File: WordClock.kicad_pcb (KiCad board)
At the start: 2 copper layers, 100 x 100 mm, 93 parts, among them J1 Conn_01x01, J2 Conn_01x01, J3 Conn_01x01, J4 Conn_01x09, J5 Conn_01x08, J6 Conn_01x08, J7 Conn_01x08, SW1 SW_Push, SW2 SW_Push, SW3 SW_Push, SW4 SW_Push, SW5 SW_Push, U1 AP1117-50, U10 NUD3124, U11 NUD3124, U12 NUD3124, U13 NUD3124, U14 NUD3124, U15 NUD3124, U16 NUD3124, U17 NUD3124, U18 NUD3124, U19 NUD3124, U2 AP1117-50, U20 NUD3124, U21 NUD3124, U22 NUD3124, U3 ARDUINO_NANO, U4 MCP7940N, U5 MCP23017, U6 MCP23017, U7 NUD3124, U8 NUD3124, U9 NUD3124, Y1 Crystal

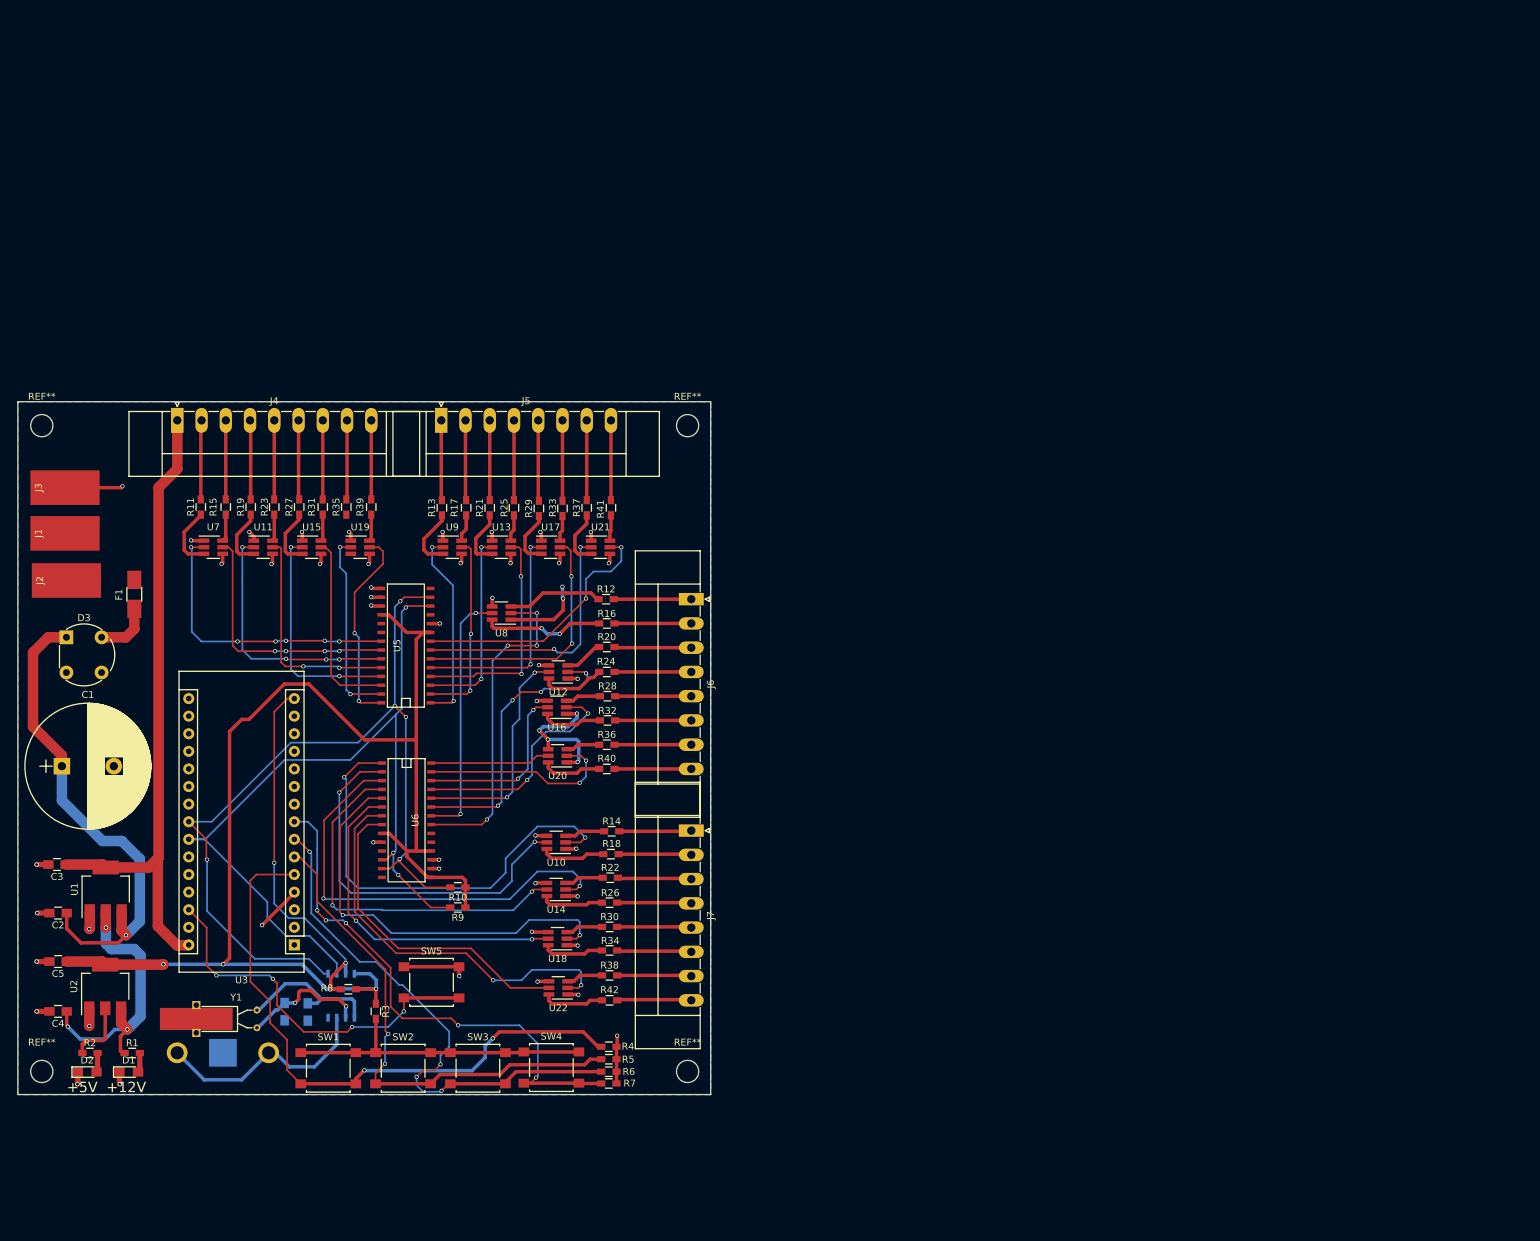
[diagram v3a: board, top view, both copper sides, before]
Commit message: Started placing and routing new board with updated schematic. Requries RTC.
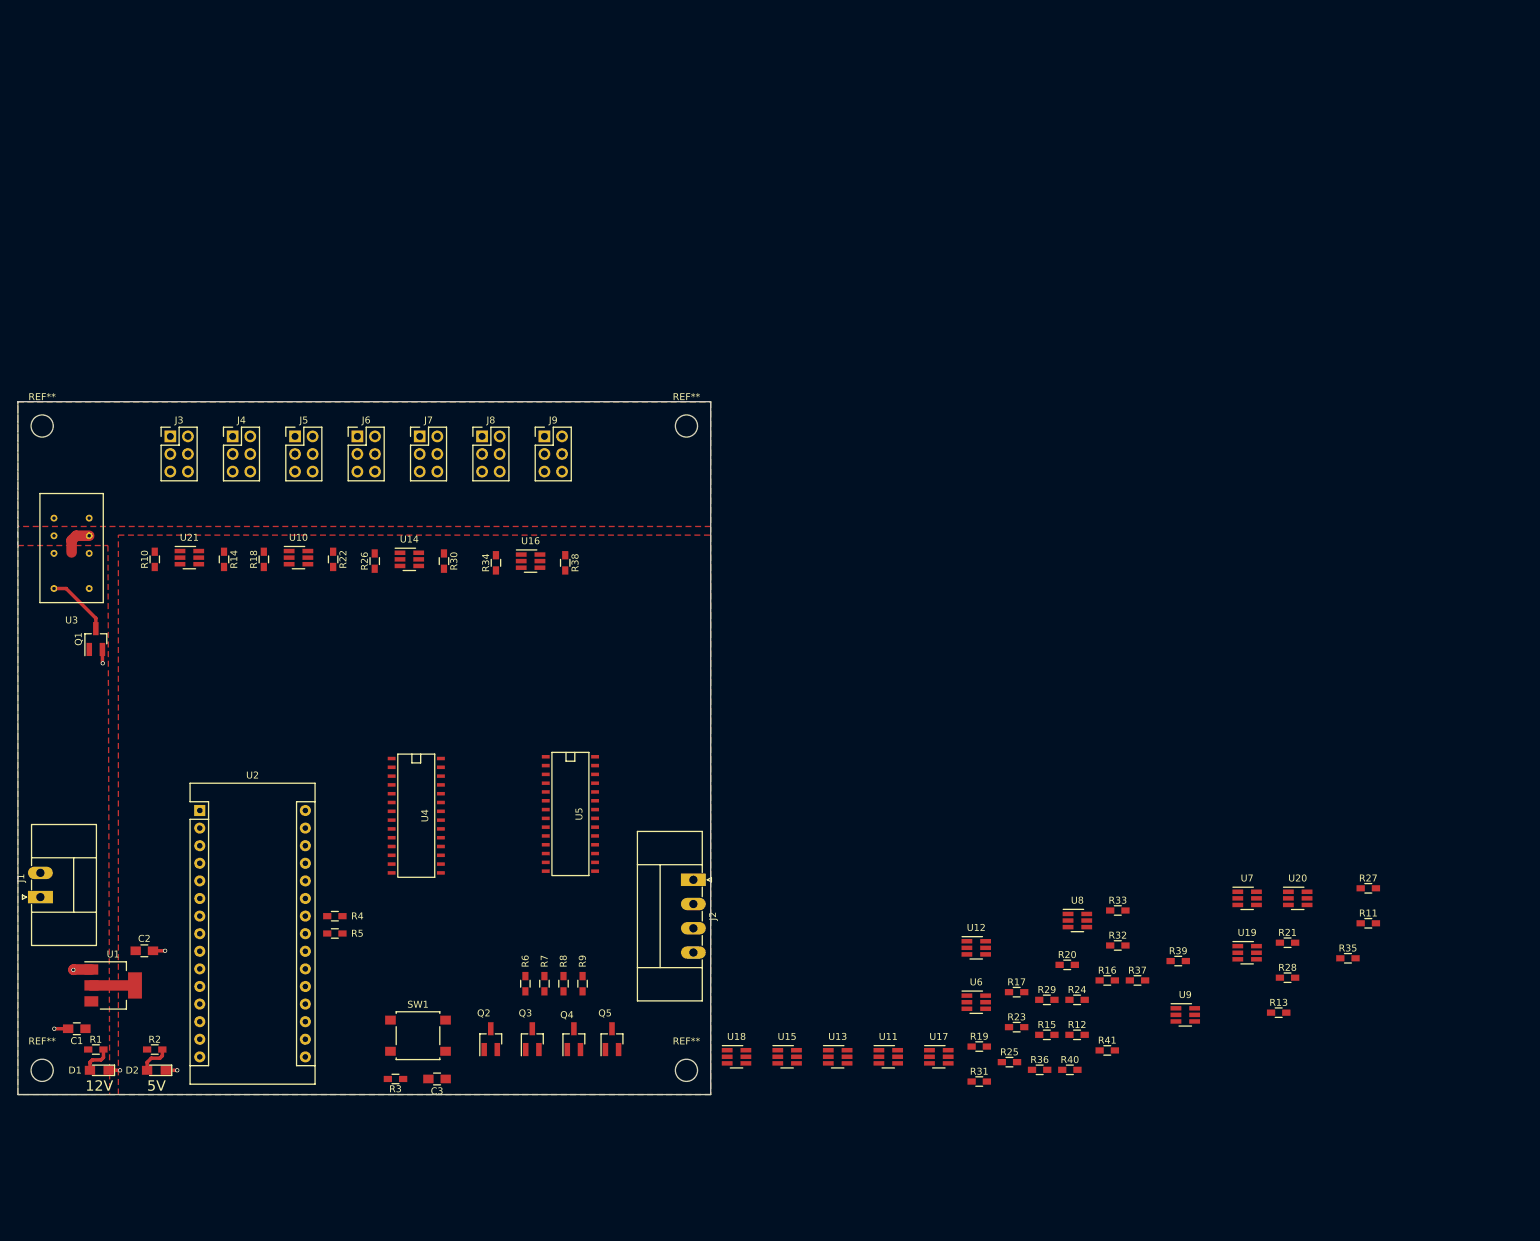
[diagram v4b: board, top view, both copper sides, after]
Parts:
- removed BT1: Battery_Cell, Battery_Holders:Keystone_3001_1x12mm-CoinCell
- removed C4, C5: 4.7uF, Capacitors_SMD:C_0805_HandSoldering
- removed C6, C7: 25pF, Capacitors_SMD:C_0805_HandSoldering
- removed D3: D_Bridge_+A-A, Diodes_THT:Diode_Bridge_Round_D8.9mm
- removed F1: Fuse, Fuse_Holders_and_Fuses:Fuse_SMD1206_HandSoldering
- removed R42: 2.7K, Resistors_SMD:R_0603_HandSoldering
- removed SW2, SW3, SW4, SW5: SW_Push, Buttons_Switches_SMD:SW_SPST_B3S-1000
- removed U22: NUD3124, TO_SOT_Packages_SMD:SOT-23-6_Handsoldering
- removed Y1: Crystal, Crystals:Crystal_AT310_d3.0mm_l10.0mm_Horizontal_1EP_style2
- added J8: Conn_02x03_Odd_Even, Pin_Headers:Pin_Header_Straight_2x03_Pitch2.54mm, F.Cu at (92.0, 30.0)
- added J9: Conn_02x03_Odd_Even, Pin_Headers:Pin_Header_Straight_2x03_Pitch2.54mm, F.Cu at (101.0, 30.0)
- added Q1: Q_NMOS_GSD, TO_SOT_Packages_SMD:SOT-23_Handsoldering, F.Cu at (36.2, 59.2)
- added Q2: Q_NMOS_GSD, TO_SOT_Packages_SMD:SOT-23_Handsoldering, F.Cu at (93.2, 117.0)
- added Q3: Q_NMOS_GSD, TO_SOT_Packages_SMD:SOT-23_Handsoldering, F.Cu at (99.2, 117.0)
- added Q4: Q_NMOS_GSD, TO_SOT_Packages_SMD:SOT-23_Handsoldering, F.Cu at (105.2, 117.0)
- added Q5: Q_NMOS_GSD, TO_SOT_Packages_SMD:SOT-23_Handsoldering, F.Cu at (110.8, 117.0)
- C1: value 1000uF -> 4.7uF; footprint Capacitors_THT:CP_Radial_D18.0mm_P7.50mm -> Capacitors_SMD:C_0805_HandSoldering
- C2: value 10uF -> 4.7uF
- C3: value 10uF -> 100nF
- J1: value Conn_01x01 -> Conn_01x02; footprint Wire_Pads:SolderWirePad_single_SMD_5x10mm -> Connectors_Phoenix:PhoenixContact_MC-GF_02x3.50mm_Angled_ThreadedFlange
- J2: value Conn_01x01 -> Conn_01x04; footprint Wire_Pads:SolderWirePad_single_SMD_5x10mm -> Connectors_Phoenix:PhoenixContact_MC-GF_04x3.50mm_Angled_ThreadedFlange
- J3: value Conn_01x01 -> Conn_02x03_Odd_Even; footprint Wire_Pads:SolderWirePad_single_SMD_5x10mm -> Pin_Headers:Pin_Header_Straight_2x03_Pitch2.54mm
- J4: value Conn_01x09 -> Conn_02x03_Odd_Even; footprint Connectors_Phoenix:PhoenixContact_MC-GF_09x3.50mm_Angled_ThreadedFlange -> Pin_Headers:Pin_Header_Straight_2x03_Pitch2.54mm
- J5, J6, J7: value Conn_01x08 -> Conn_02x03_Odd_Even; footprint Connectors_Phoenix:PhoenixContact_MC-GF_08x3.50mm_Angled_ThreadedFlange -> Pin_Headers:Pin_Header_Straight_2x03_Pitch2.54mm
- R10: value 4.7K -> 2.7K
- R3, R6, R7, R9: value 4.7K -> 10K
- U2: value AP1117-50 -> ARDUINO_NANO; footprint TO_SOT_Packages_SMD:SOT-223-3_TabPin2 -> Modules:Arduino_Nano
- U3: value ARDUINO_NANO -> E2C-12NU; footprint Modules:Arduino_Nano -> CustomFootprint:EC2-12NU
- U4: value MCP7940N -> MCP23017; footprint SMD_Packages:SOIC-8-N -> SMD_Packages:SOIC-28; moved to F.Cu
- U6: value MCP23017 -> NUD3124; footprint SMD_Packages:SOIC-28 -> TO_SOT_Packages_SMD:SOT-23-6_Handsoldering
- moved R11 178.9 mm to (219.9, 100.3), turned to 0 degrees
- moved R27 163.8 mm to (219.9, 95.2), turned to 0 degrees
- moved R35 158.6 mm to (217.0, 105.3), turned to 0 degrees
- moved U7 157.6 mm to (202.4, 96.7)
- moved R13 141.1 mm to (207.0, 113.2), turned to 0 degrees
- moved R15 140.9 mm to (173.5, 116.4), turned to 0 degrees
- moved U19 140.8 mm to (202.4, 104.5)
- moved R39 133.6 mm to (192.5, 105.7), turned to 0 degrees
- moved REF** 131.8 mm to (28.5, 28.5)
- moved REF** 131.7 mm to (28.5, 121.5)
- moved R21 131.2 mm to (208.3, 103.1), turned to 0 degrees
- moved R19 130.9 mm to (163.8, 118.1), turned to 0 degrees
- moved R23 130.8 mm to (169.2, 115.3), turned to 0 degrees
- moved R31 125.9 mm to (163.8, 123.1), turned to 0 degrees
- moved U9 125.5 mm to (193.5, 113.5)
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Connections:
- net OUT1 renamed OUT_17
- net OUT10 renamed OUT_26
- net OUT11 renamed OUT_27
- net OUT12 renamed OUT_28
- net OUT13 renamed OUT_29
- net OUT14 renamed OUT_30
- net OUT15 renamed OUT_31
- net OUT16 renamed OUT_32
- net OUT2 renamed OUT_18
- net OUT3 renamed OUT_19
- net OUT4 renamed OUT_20
- net OUT5 renamed OUT_21
- net OUT6 renamed OUT_22
- net OUT7 renamed OUT_23
- net OUT8 renamed OUT_24
- net OUT9 renamed OUT_25
- C1 pad 1: Net-(C1-Pad1) -> +12V
- C2 pad 1: Net-(C1-Pad1) -> +5V
- C3 pad 1: +12V -> +5V
- C3 pad 2: GND -> ButtonRead
- J1 pad 1: AC+ -> +12V
- J2 pad 1: AC- -> PWM_1_OUTPUT
- J3 pad 1: GND -> LED_PWR
- J4 pad 1: +12V -> LED_PWR
- J4 pad 2: LED1 -> LED8
- J4 pad 3: LED2 -> LED6
- J4 pad 4: LED3 -> LED9
- J4 pad 5: LED4 -> LED7
- J4 pad 6: LED5 -> LED10
- J5 pad 1: LED9 -> LED_PWR
- J5 pad 2: LED10 -> LED13
- J5 pad 4: LED12 -> LED14
- J5 pad 5: LED13 -> LED12
- J5 pad 6: LED14 -> LED15
- J6 pad 1: LED17 -> LED_PWR
- J6 pad 3: LED19 -> LED16
- J6 pad 4: LED20 -> LED19
- J6 pad 5: LED21 -> LED17
- J6 pad 6: LED22 -> LED20
- J7 pad 1: LED25 -> LED_PWR
- J7 pad 2: LED26 -> LED23
- J7 pad 3: LED27 -> LED21
- J7 pad 4: LED28 -> LED24
- J7 pad 5: LED29 -> LED22
- J7 pad 6: LED30 -> LED25
- R10 pad 1: +5V -> Net-(R10-Pad1)
- R10 pad 2: SDA -> LED1
- R11 pad 2: LED1 -> LED17
- R12 pad 2: LED17 -> LED9
- R13 pad 2: LED9 -> LED25
- R14 pad 1: Net-(R14-Pad1) -> LED2
- R14 pad 2: LED25 -> Net-(R14-Pad2)
- R15 pad 1: LED2 -> LED18
- R16 pad 1: LED18 -> LED10
- R17 pad 1: LED10 -> LED26
- R18 pad 1: LED26 -> Net-(R18-Pad1)
- R18 pad 2: Net-(R18-Pad2) -> LED3
- R19 pad 2: LED3 -> LED19
- R20 pad 2: LED19 -> LED11
- R21 pad 2: LED11 -> LED27
- R22 pad 1: Net-(R22-Pad1) -> LED4
- R22 pad 2: LED27 -> Net-(R22-Pad2)
- R23 pad 1: LED4 -> LED20
- R24 pad 1: LED20 -> LED12
- R25 pad 1: LED12 -> LED28
- R26 pad 1: LED28 -> Net-(R26-Pad1)
- R26 pad 2: Net-(R26-Pad2) -> LED5
- R27 pad 2: LED5 -> LED21
- R28 pad 2: LED21 -> LED13
- R29 pad 2: LED13 -> LED29
- R3 pad 1: +5V -> ButtonRead
- R3 pad 2: Net-(R3-Pad2) -> GND
- R30 pad 1: Net-(R30-Pad1) -> LED6
- R30 pad 2: LED29 -> Net-(R30-Pad2)
- R31 pad 1: LED6 -> LED22
- R32 pad 1: LED22 -> LED14
- R33 pad 1: LED14 -> LED30
- R34 pad 1: LED30 -> Net-(R34-Pad1)
- R34 pad 2: Net-(R34-Pad2) -> LED7
- R35 pad 2: LED7 -> LED23
- R36 pad 2: LED23 -> LED15
- R37 pad 2: LED15 -> LED31
- R38 pad 1: Net-(R38-Pad1) -> LED8
- R38 pad 2: LED31 -> Net-(R38-Pad2)
- R39 pad 1: LED8 -> LED24
- R4 pad 1: Net-(R4-Pad1) -> +5V
- R4 pad 2: GND -> SCL
- R40 pad 1: LED24 -> LED16
- R41 pad 1: LED16 -> LED32
- R5 pad 1: Net-(R5-Pad1) -> +5V
- R5 pad 2: GND -> SDA
- R6 pad 1: Net-(R6-Pad1) -> PWM_1_OUTPUT
- R6 pad 2: GND -> Net-(Q2-Pad3)
- R7 pad 1: Net-(R7-Pad1) -> PWM_2_OUTPUT
- R7 pad 2: GND -> Net-(Q3-Pad3)
- R8 pad 1: MFP -> PWM_3_OUTPUT
- R8 pad 2: +5V -> Net-(Q4-Pad3)
- R9 pad 1: +5V -> PWM_4_OUTPUT
- R9 pad 2: SCL -> Net-(Q5-Pad3)
- SW1 pad 1: Net-(R3-Pad2) -> ButtonRead
- SW1 pad 2: Net-(R4-Pad1) -> +5V
- U1 pad 2: +12V -> +5V
- U1 pad 3: Net-(C1-Pad1) -> +12V
- U10 pad 2: OUT25 -> OUT_3
- U10 pad 3: Net-(R14-Pad1) -> Net-(R18-Pad1)
- U10 pad 5: OUT26 -> OUT_4
- U10 pad 6: Net-(R18-Pad2) -> Net-(R22-Pad2)
- U12 pad 2: OUT19 -> OUT_11
- U12 pad 5: OUT20 -> OUT_12
- U14 pad 2: OUT27 -> OUT_5
- U14 pad 3: Net-(R22-Pad1) -> Net-(R26-Pad1)
- U14 pad 5: OUT28 -> OUT_6
- U14 pad 6: Net-(R26-Pad2) -> Net-(R30-Pad2)
- U16 pad 2: OUT21 -> OUT_13
- U16 pad 5: OUT22 -> OUT_14
- U18 pad 2: OUT29 -> OUT_7
- U18 pad 3: Net-(R30-Pad1) -> Net-(R34-Pad1)
- U18 pad 5: OUT30 -> OUT_8
- U18 pad 6: Net-(R34-Pad2) -> Net-(R38-Pad2)
- U2 pad 1: GND -> Net-(U2-Pad1)
- U2 pad 2: +5V -> Net-(U2-Pad2)
- U2 pad 3: +12V -> Net-(U2-Pad3)
- U20 pad 2: OUT23 -> OUT_15
- U20 pad 5: OUT24 -> OUT_16
- U3 pad 1: Net-(U3-Pad1) -> +12V
- U3 pad 4: GND -> +12V
- U3 pad 5: Net-(R4-Pad1) -> LED_PWR
- U3 pad 8: Net-(R7-Pad1) -> Net-(U3-Pad8)
- U4 pad 1: Net-(C6-Pad2) -> OUT_9
- U4 pad 2: Net-(C7-Pad2) -> OUT_10
- U4 pad 3: Net-(BT1-Pad1) -> OUT_11
- U4 pad 4: GND -> OUT_12
- U4 pad 5: SDA -> OUT_13
- U4 pad 6: SCL -> OUT_14
- U4 pad 7: MFP -> OUT_15
- U4 pad 8: +5V -> OUT_16
- U5 pad 15: GND -> +5V
- U5 pad 16: GND -> +5V
- U5 pad 17: GND -> +5V
- U6 pad 1: OUT25 -> GND
- U6 pad 2: OUT26 -> OUT_1
- U6 pad 3: OUT27 -> Net-(R10-Pad1)
- U6 pad 4: OUT28 -> GND
- U6 pad 5: OUT29 -> OUT_2
- U6 pad 6: OUT30 -> Net-(R14-Pad2)
- U8 pad 2: OUT17 -> OUT_9
- U8 pad 5: OUT18 -> OUT_10
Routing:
- net +5V: track 196.5 -> 6.30 mm, vias 3 -> 0
- net +12V: track 135.5 -> 4.56 mm, vias 3 -> 0
- net SDA: track 127.4 -> 0.00 mm, vias 5 -> 0
- net SCL: track 123.7 -> 0.00 mm, vias 3 -> 0
- net GND: track 131.3 -> 11.7 mm, vias 53 -> 6
- net Net-(R4-Pad1): track 88.3 -> 0.00 mm, vias 2 -> 0
- net Net-(R6-Pad1): track 77.9 -> 0.00 mm, vias 4 -> 0
- net Net-(R7-Pad1): track 77.5 -> 0.00 mm, vias 5 -> 0
- net Net-(R5-Pad1): track 73.6 -> 0.00 mm, vias 2 -> 0
- net Net-(C1-Pad1): track 71.2 -> 0.00 mm, vias 1 -> 0
- net OUT25: track 64.6 -> 0.00 mm, vias 2 -> 0
- net OUT27: track 64.6 -> 0.00 mm, vias 2 -> 0
- net OUT29: track 60.8 -> 0.00 mm, vias 2 -> 0
- net OUT31: track 58.3 -> 0.00 mm, vias 2 -> 0
- net OUT26: track 55.3 -> 0.00 mm, vias 2 -> 0
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- added copper zone on F.Cu, net +12V
- added copper zone on F.Cu, net +5V
- added copper zone on F.Cu, net LED_PWR
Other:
- board text added: "12V"
- board text added: "5V"
- board text removed: "+12V"
- board text removed: "+5V"

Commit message: Finished layout and began routing board.
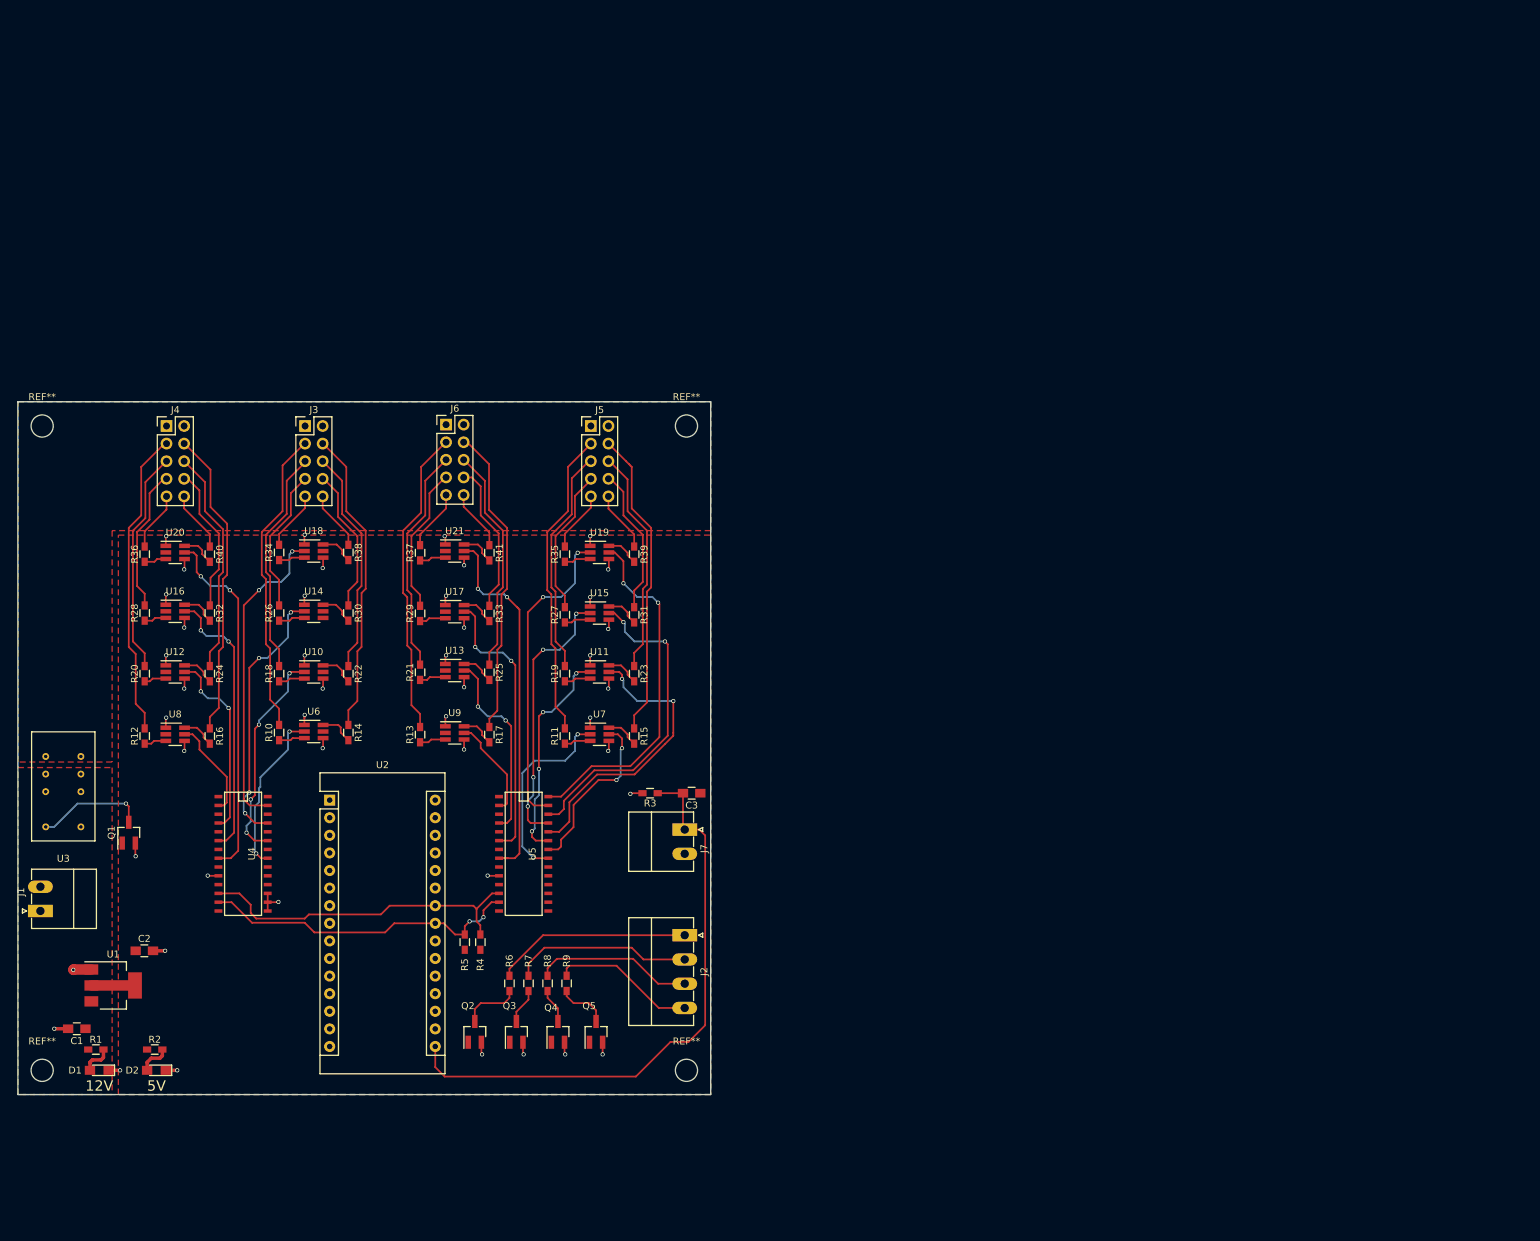
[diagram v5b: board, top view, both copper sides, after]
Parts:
- removed J8, J9: Conn_02x03_Odd_Even, Pin_Headers:Pin_Header_Straight_2x03_Pitch2.54mm
- removed SW1: SW_Push, Buttons_Switches_SMD:SW_SPST_B3S-1000
- J1: footprint Connectors_Phoenix:PhoenixContact_MC-GF_02x3.50mm_Angled_ThreadedFlange -> Connectors_Phoenix:PhoenixContact_MC-G_02x3.50mm_Angled
- J2: footprint Connectors_Phoenix:PhoenixContact_MC-GF_04x3.50mm_Angled_ThreadedFlange -> Connectors_Phoenix:PhoenixContact_MC-G_04x3.50mm_Angled
- J3, J4, J5, J6: value Conn_02x03_Odd_Even -> Conn_02x05_Top_Bottom; footprint Pin_Headers:Pin_Header_Straight_2x03_Pitch2.54mm -> Pin_Headers:Pin_Header_Straight_2x05_Pitch2.54mm
- J7: value Conn_02x03_Odd_Even -> Conn_01x02; footprint Pin_Headers:Pin_Header_Straight_2x03_Pitch2.54mm -> Connectors_Phoenix:PhoenixContact_MC-G_02x3.50mm_Angled
- moved R28 173.2 mm to (43.3, 55.5), turned to 90 degrees
- moved U20 169.5 mm to (47.7, 46.8)
- moved R36 149.1 mm to (43.3, 47.0), turned to 90 degrees
- moved R40 144.7 mm to (52.7, 47.0), turned to 270 degrees
- moved R12 141.3 mm to (43.3, 73.2), turned to 90 degrees
- moved R20 139.6 mm to (43.3, 64.2), turned to 90 degrees
- moved R32 139.6 mm to (52.7, 55.5), turned to 270 degrees
- moved R16 134.3 mm to (52.7, 73.2), turned to 270 degrees
- moved R24 133.7 mm to (52.7, 64.2), turned to 270 degrees
- moved U8 133.0 mm to (47.7, 73.0)
- moved R21 131.2 mm to (83.0, 64.0), turned to 90 degrees
- moved R13 130.3 mm to (83.0, 73.0), turned to 90 degrees
- moved R35 127.2 mm to (104.0, 47.0), turned to 90 degrees
- moved R27 122.5 mm to (104.0, 55.8), turned to 90 degrees
- moved U12 122.3 mm to (47.7, 64.0)
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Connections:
- J3 pad 2: LED3 -> LED_PWR
- J3 pad 4: LED4 -> LED2
- J3 pad 5: LED2 -> LED3
- J3 pad 6: LED5 -> LED4
- J4 pad 2: LED8 -> LED_PWR
- J4 pad 3: LED6 -> LED9
- J4 pad 4: LED9 -> LED10
- J4 pad 5: LED7 -> LED11
- J4 pad 6: LED10 -> LED12
- J5 pad 2: LED13 -> LED_PWR
- J5 pad 3: LED11 -> LED17
- J5 pad 4: LED14 -> LED18
- J5 pad 5: LED12 -> LED19
- J5 pad 6: LED15 -> LED20
- J6 pad 2: LED18 -> LED_PWR
- J6 pad 3: LED16 -> LED25
- J6 pad 4: LED19 -> LED26
- J6 pad 5: LED17 -> LED27
- J6 pad 6: LED20 -> LED28
- J7 pad 1: LED_PWR -> ButtonRead
- J7 pad 2: LED23 -> +5V
- U2 pad 30: +12V -> +5V
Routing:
- net ButtonRead: track 0.00 -> 85.3 mm
- net GND: track 11.7 -> 72.0 mm, vias 6 -> 45
- net OUT_32: track 0.00 -> 54.0 mm, vias 0 -> 2
- net OUT_16: track 0.00 -> 51.6 mm, vias 0 -> 2
- net OUT_24: track 0.00 -> 51.1 mm, vias 0 -> 2
- net SCL: track 0.00 -> 48.5 mm
- net OUT_22: track 0.00 -> 46.9 mm, vias 0 -> 2
- net SDA: track 0.00 -> 46.7 mm, vias 0 -> 2
- net OUT_7: track 0.00 -> 45.5 mm, vias 0 -> 2
- net OUT_23: track 0.00 -> 45.2 mm, vias 0 -> 2
- net LED26: track 0.00 -> 45.1 mm
- net LED17: track 0.00 -> 44.8 mm
- net LED10: track 0.00 -> 44.7 mm
- net LED25: track 0.00 -> 44.7 mm
- net LED18: track 0.00 -> 44.7 mm
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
